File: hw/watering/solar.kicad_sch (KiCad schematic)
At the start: 7 parts, among them U2 DRV8220DSG

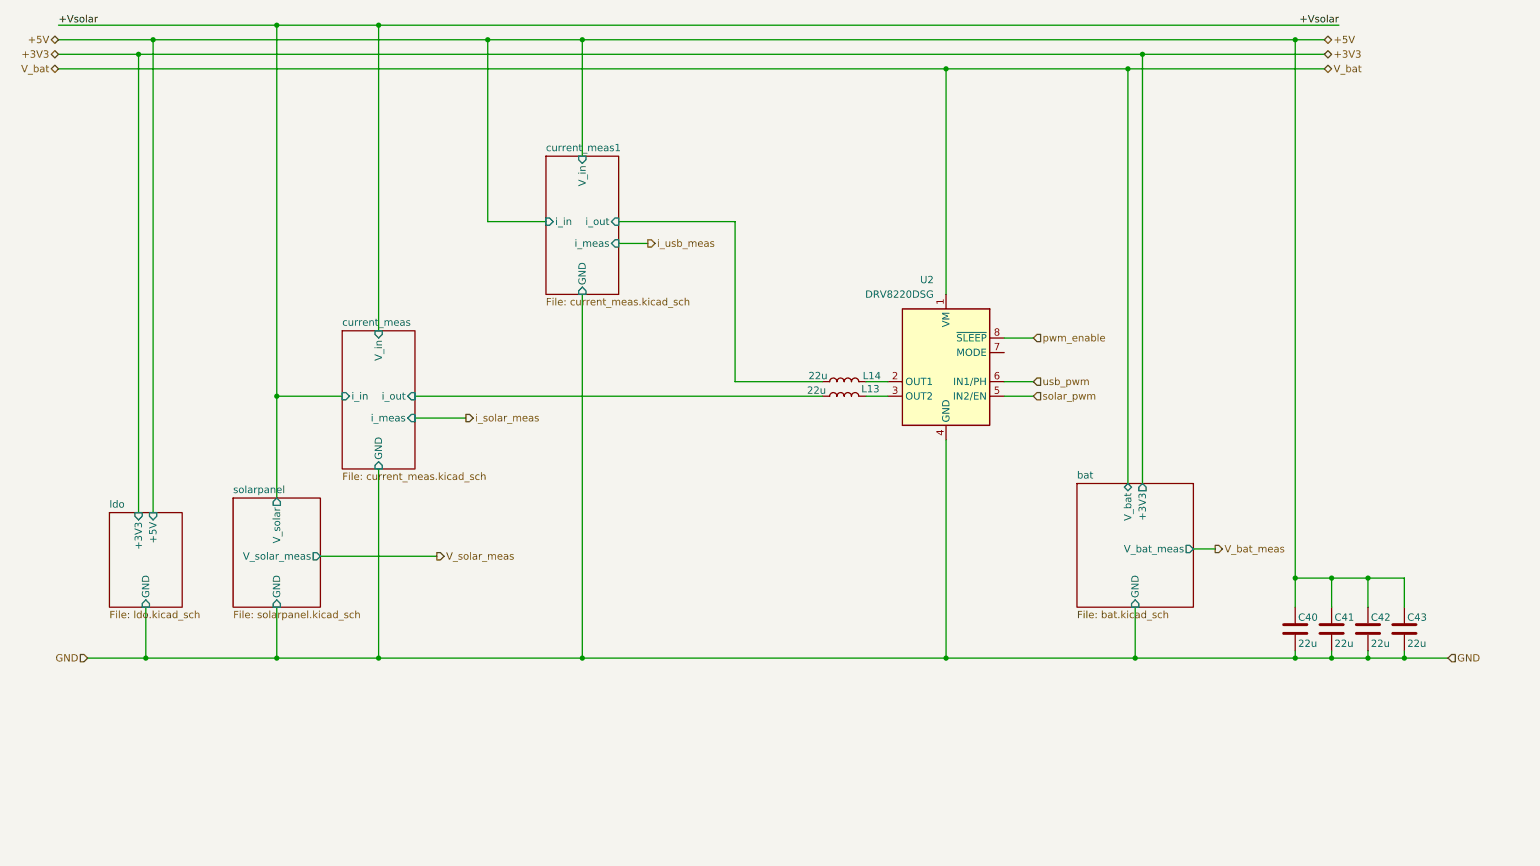
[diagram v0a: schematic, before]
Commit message: reduced pcb size
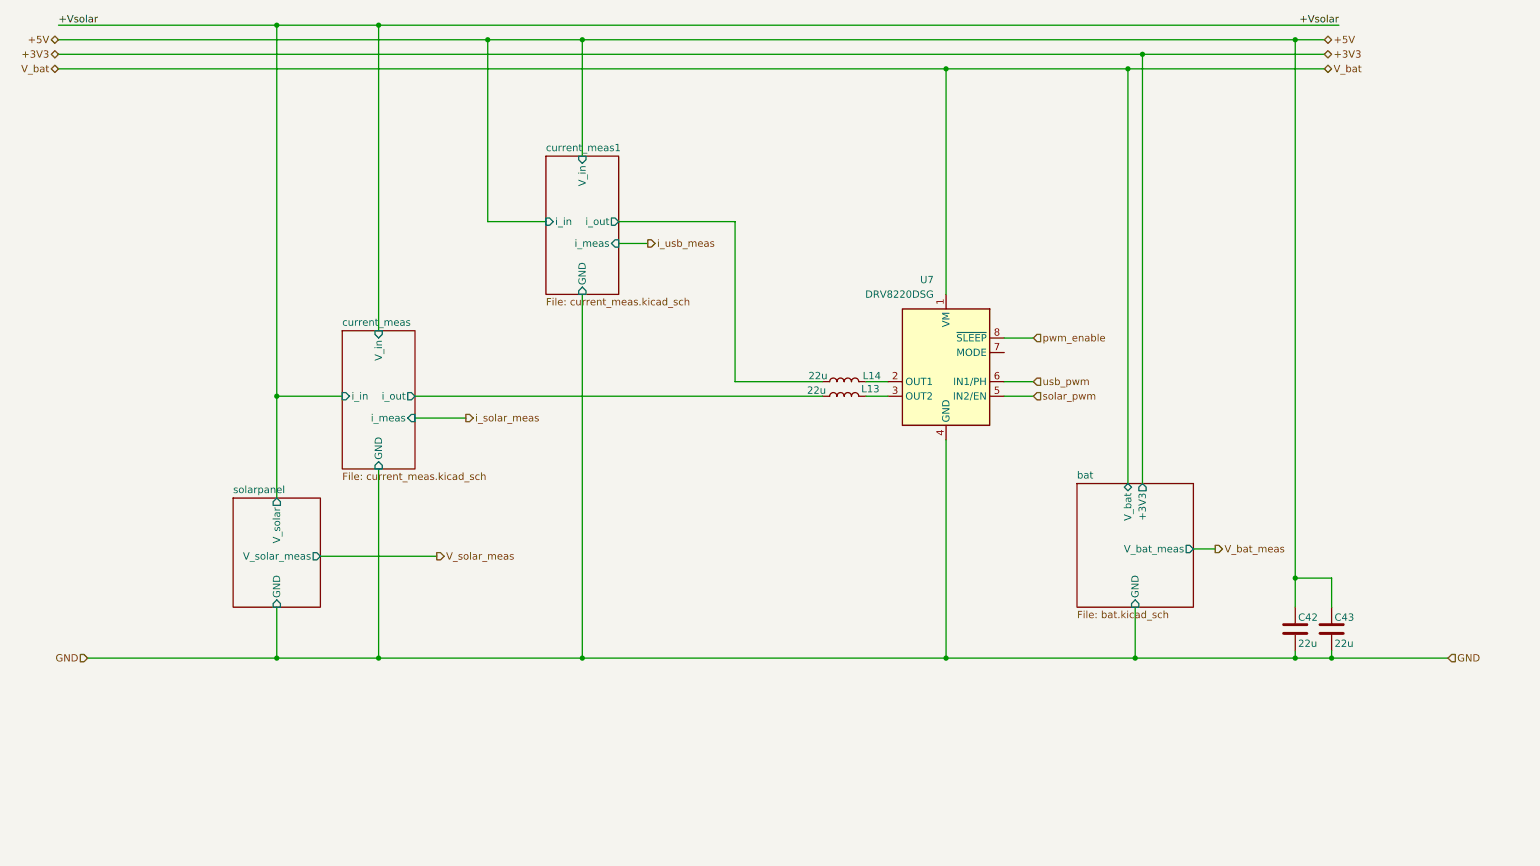
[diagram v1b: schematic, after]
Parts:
- removed C40, C41: 22u, Capacitor_SMD:C_1206_3216Metric, symbol Device:C
- removed U2: DRV8220DSG, Package_SON:WSON-8-1EP_2x2mm_P0.5mm_EP0.9x1.6mm, symbol Driver_Motor:DRV8220DSG
- added U7: DRV8220DSG, Package_SON:Texas_DSG0008A_WSON-8-1EP_2x2mm_P0.5mm_EP0.9x1.6mm, symbol Driver_Motor:DRV8220DSG
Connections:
- net GND: now also U7.4 (GND), U7.9 (GND)
- net V_bat: now also U7.1 (VM)
- net pwm_enable: now also U7.8 (~{SLEEP})
- net solar_pwm: now also U7.5 (IN2/EN)
- net usb_pwm: now also U7.6 (IN1/PH)
- net at L14.1: now also U7.2 (OUT1)
- net at L13.1: now also U7.3 (OUT2)
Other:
- removed sheet ldo
- moved on the sheet: C42, C43

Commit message: - hw   - rewired power input for battery   - some first placing of parts on pcb but no routing - sw   - added example http server from examples to server.cpp, not compilable yet
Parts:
- removed C42, C43: 22u, Capacitor_SMD:C_1206_3216Metric, symbol Device:C
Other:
- sheet bat ports: added power_enable; removed none
- note added: "solar battery charging"
- note added: "usb battery charging"
- moved on the sheet: L13, L14, U7
